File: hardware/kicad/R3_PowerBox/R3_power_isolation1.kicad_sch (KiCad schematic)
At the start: 13 parts, among them U3 RS3E-0505S/H3

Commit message: Finalize R3 PowerBox pre-placement corrections
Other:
- moved on the sheet: C30, C31, C32, C33, C34, C35, FB2, FB3, U3

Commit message: Finalize R3 PowerBox pre-routing placement
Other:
- moved on the sheet: FB3

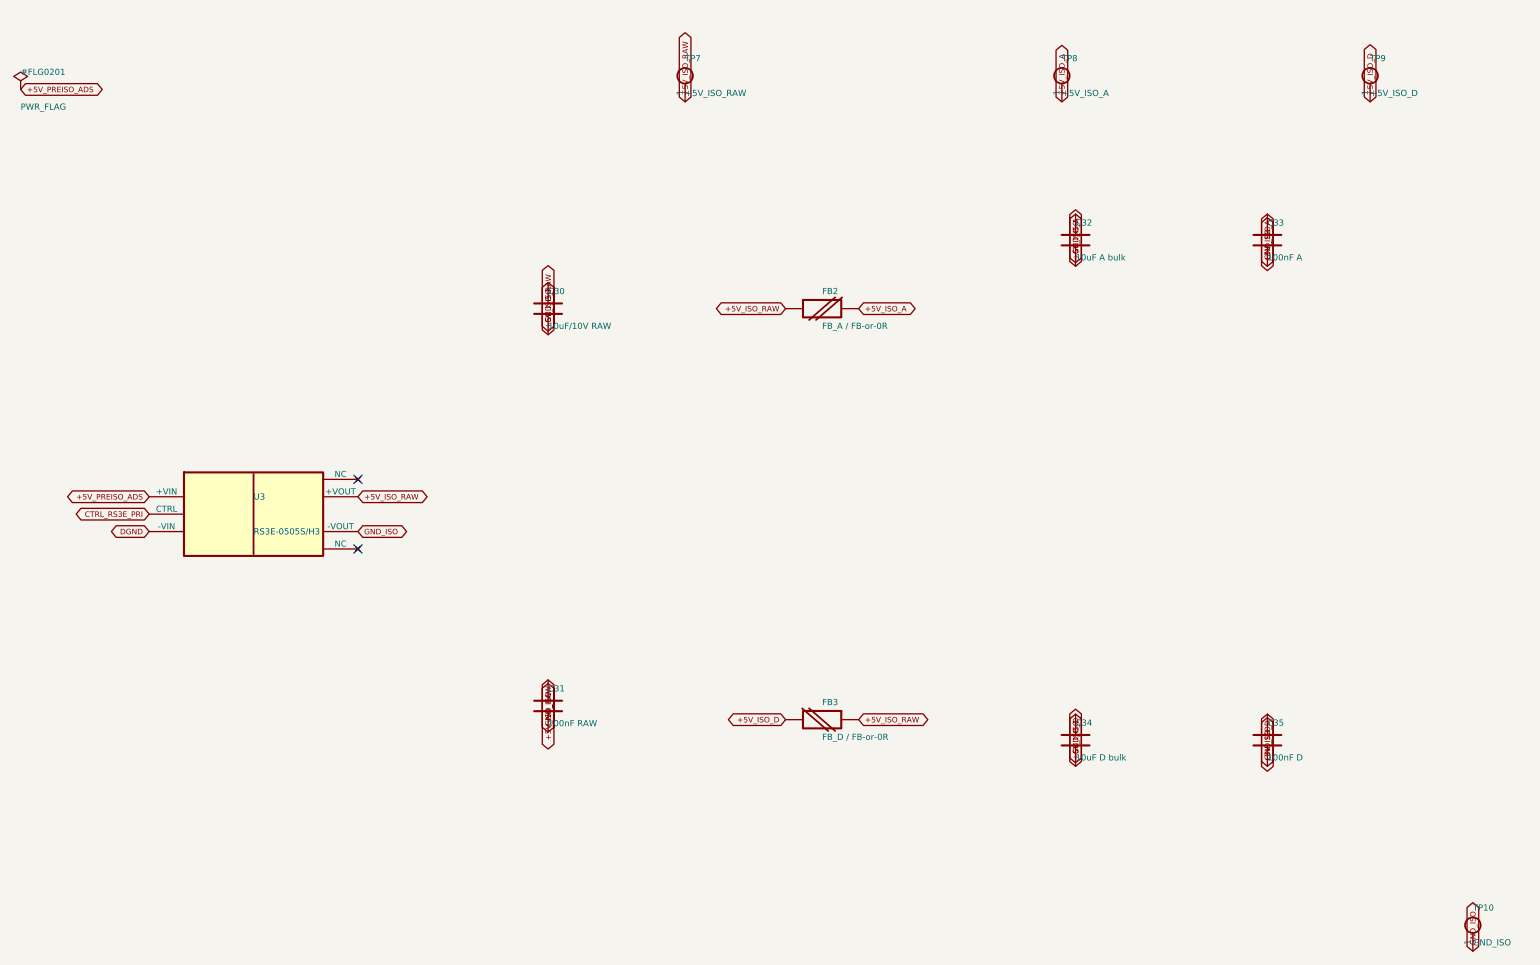
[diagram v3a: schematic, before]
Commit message: Finalize R3 PowerBox mechanical interconnect
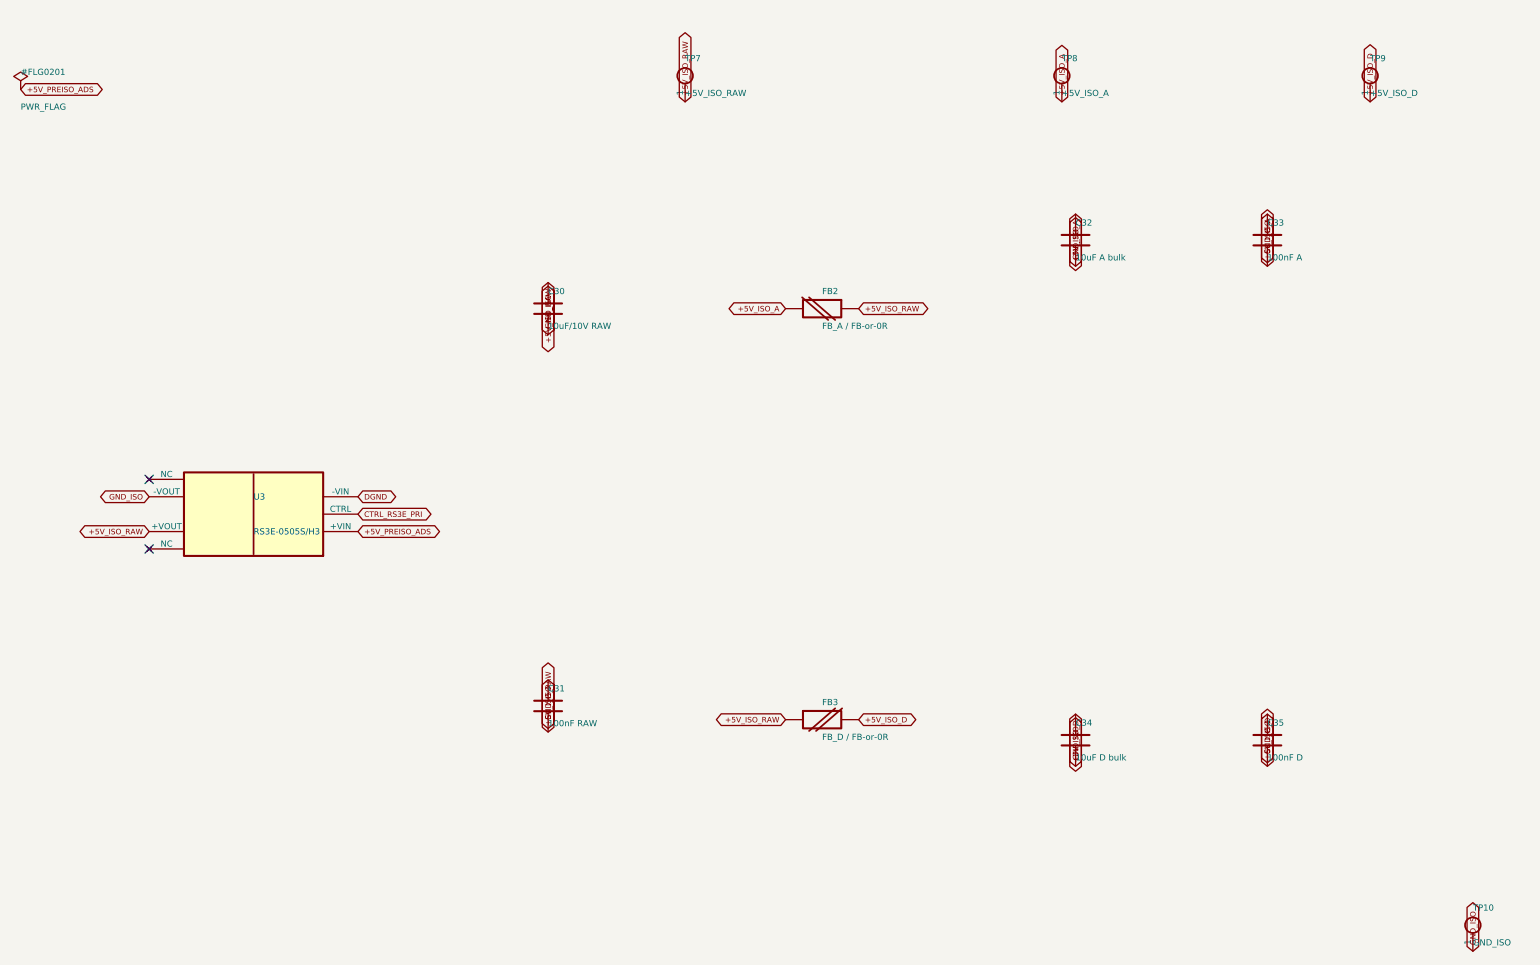
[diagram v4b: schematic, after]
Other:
- moved on the sheet: FB2, FB3, U3

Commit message: Finish R3 PowerBox routing checkpoint F and verification
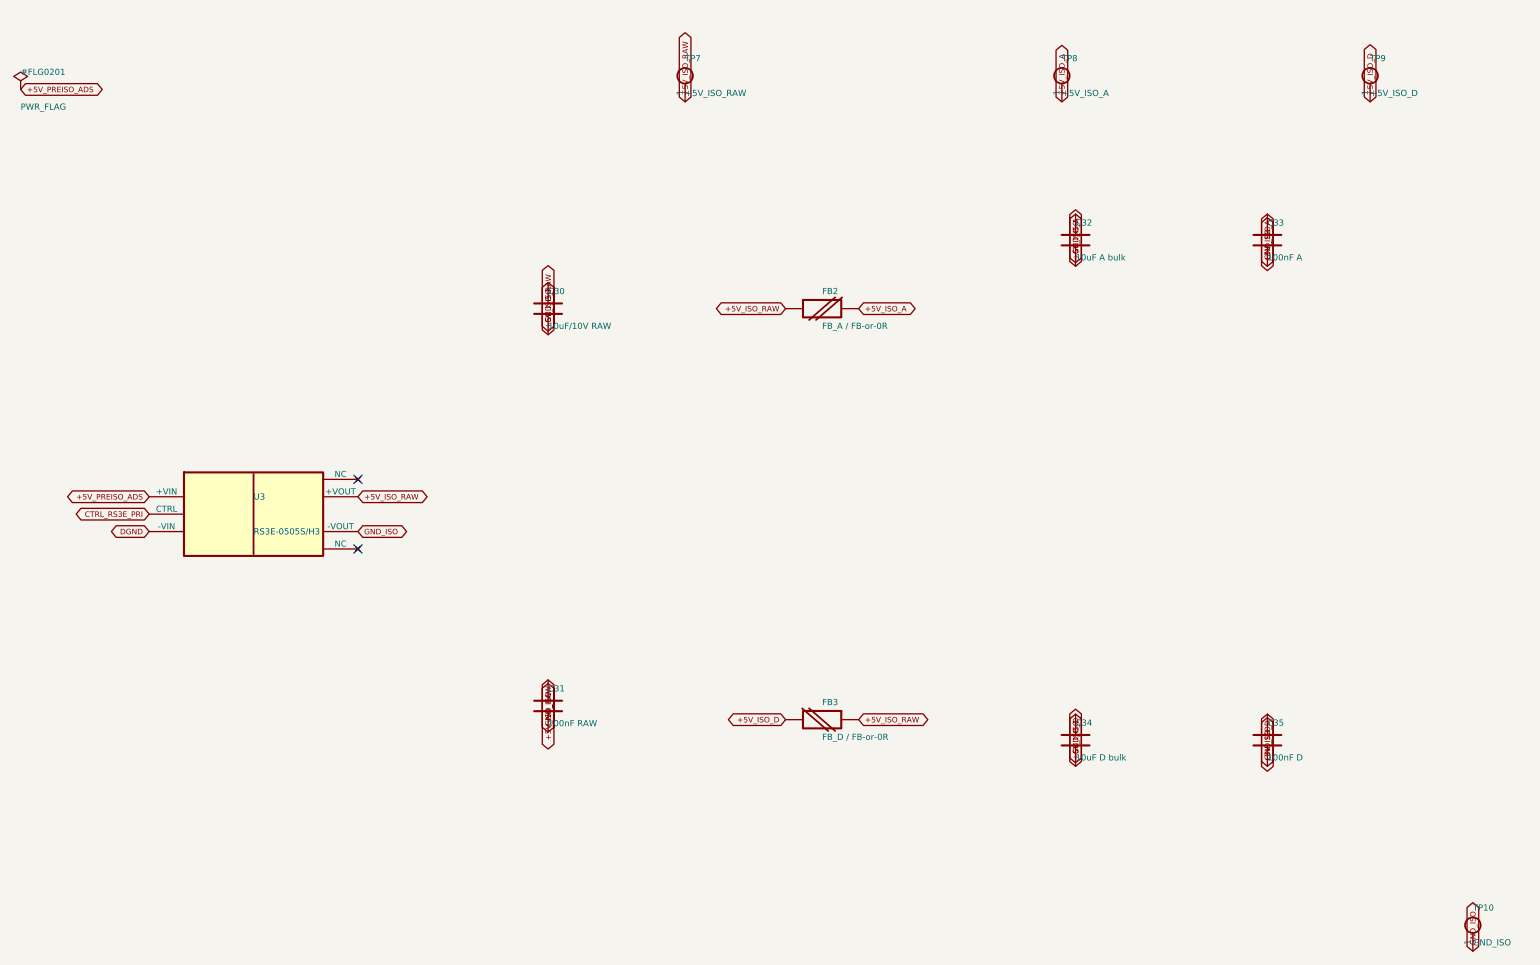
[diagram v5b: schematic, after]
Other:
- moved on the sheet: FB2, FB3, U3

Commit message: Rev.A review fixes: initial schematic and component corrections
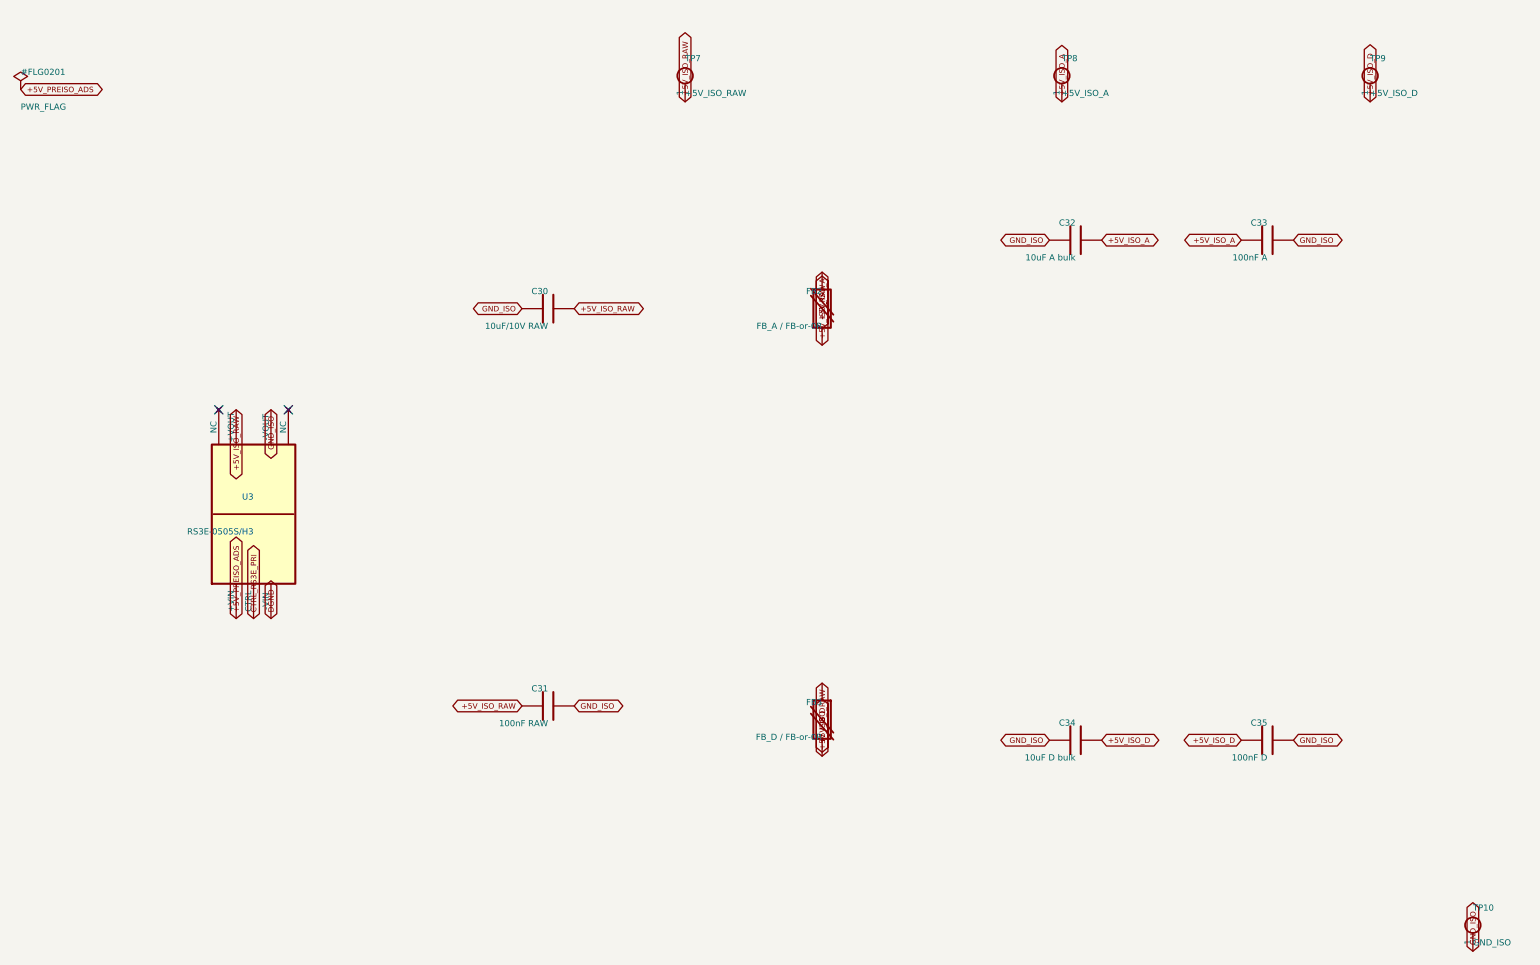
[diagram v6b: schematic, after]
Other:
- moved on the sheet: C30, C31, C32, C33, C34, C35, FB2, FB3, U3

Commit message: Rev.A review fixes: local charger power-stage reroute checkpoint
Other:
- moved on the sheet: C30, C31, C32, C33, C34, C35, FB2, FB3, U3

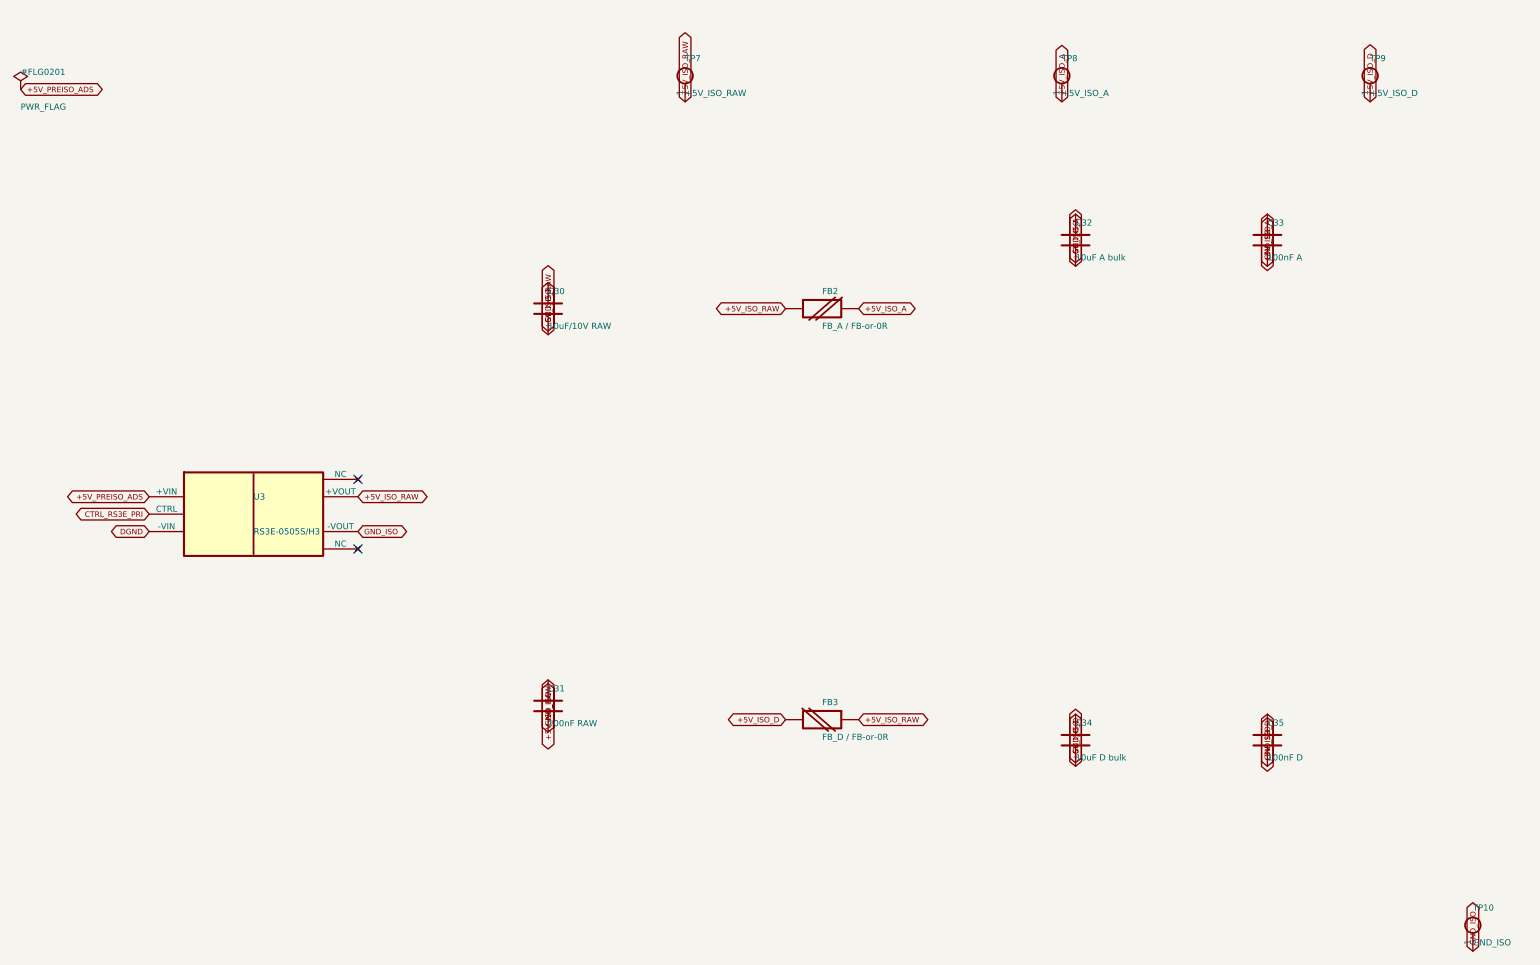
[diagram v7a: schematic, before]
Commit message: Rev.A review fixes: final CAD verification and documented hardware gates
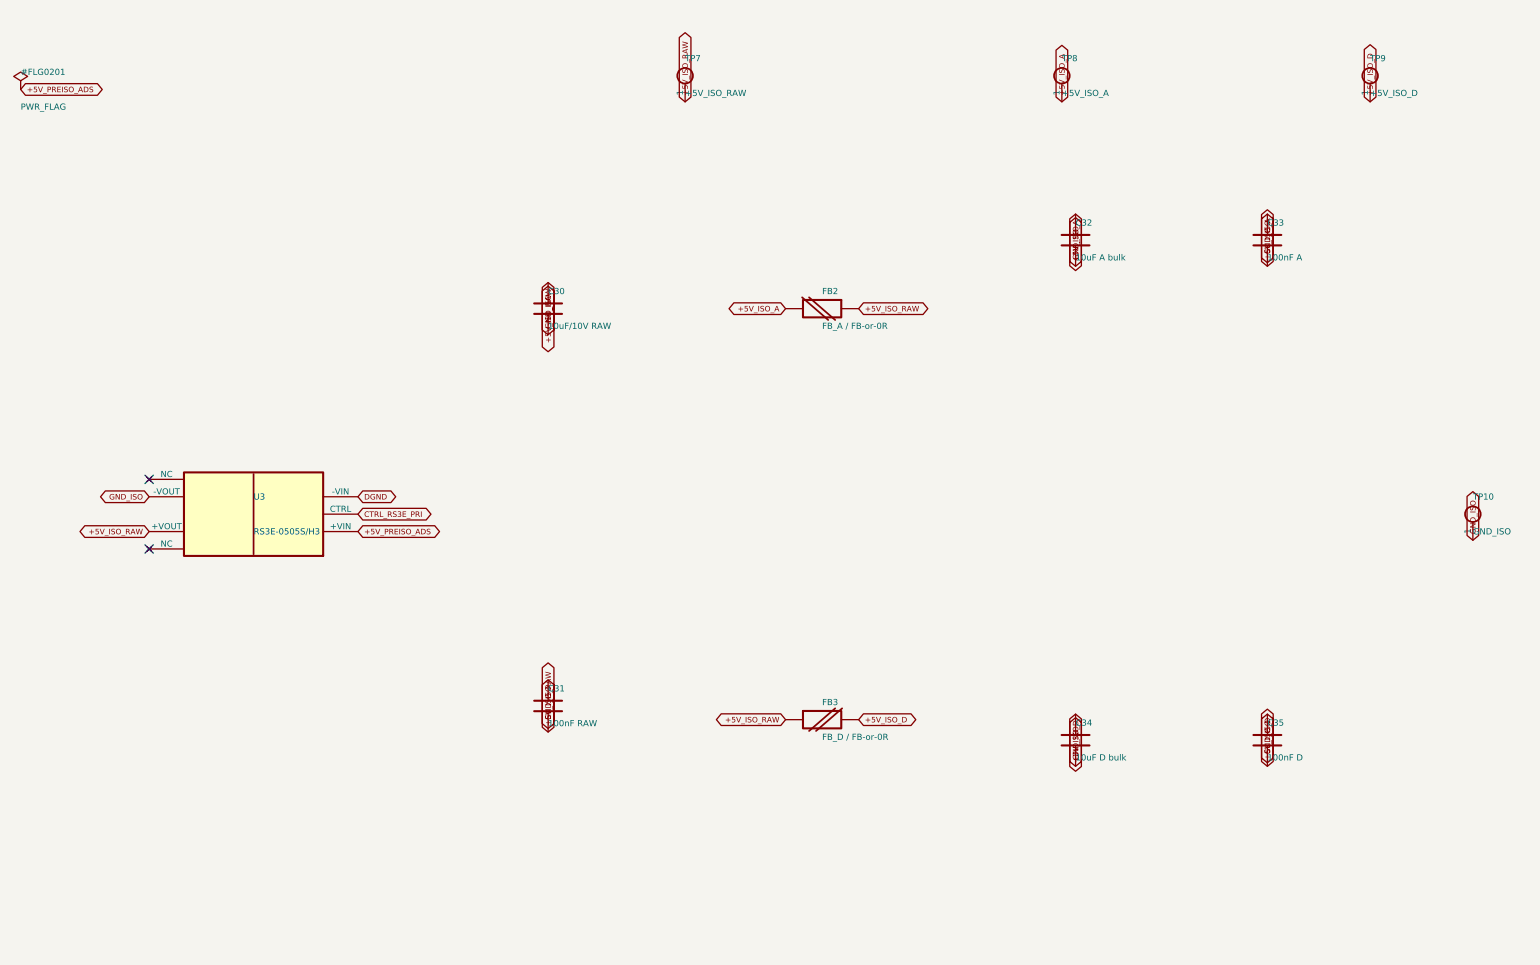
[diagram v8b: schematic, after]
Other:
- moved on the sheet: FB2, FB3, TP10, U3
